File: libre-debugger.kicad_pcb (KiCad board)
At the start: 2 copper layers, 50 x 60 mm, 82 parts, among them J1 USB_C_Receptacle_USB2.0, J2 Conn_ST_STDC14, J4 Conn_01x16, Q1 2N7002, SW1 SW_SPDT, SW2 SW_Push, U1 FT2232H, U10 74LVC1G125, U11 74LVC1G125, U12 74LVC1G125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

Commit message: Replace LDO: MIC5504 -> XC6026
Available on JLCPCB as Basic Part.
Many alternative MPNs available for this new footprint, so not an issue.
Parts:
- U2: value MIC5504-3.3YM5 -> XC6206PxxxMR; footprint Package_TO_SOT_SMD:SOT-23-5 -> Package_TO_SOT_SMD:SOT-23
- moved U2 0.30 mm to (134.4, 60.1), turned to 180 degrees
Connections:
- U2 pad 1: +5V -> GND
- U2 pad 2: GND -> +3V3
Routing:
- net +5V: track 7.08 -> 3.69 mm
- net +3V3: track 14.6 -> 13.0 mm

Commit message: Use 4u7 caps for LDO input and output too
Minimum size recommended is 1uF input and 1uF output.
But given capacitance derating vs DC voltage, it is probably
a good idea to go for a higher value. That reduces the number
of MPNs too.
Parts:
- C1, C2: value 1u -> 4u7
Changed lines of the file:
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@@
       (effects (font (size 0.8 0.8) (thickness 0.15)))
     )
-    (fp_text value "1u" (at 0 1.43 90) (layer "F.Fab") hide
+    (fp_text value "4u7" (at 0 1.43 90) (layer "F.Fab") hide
       (effects (font (size 0.5 0.5) (thickness 0.15)))
     )
@@
       (effects (font (size 0.8 0.8) (thickness 0.15)))
     )
-    (fp_text value "1u" (at 0 1.43 90) (layer "F.Fab") hide
+    (fp_text value "4u7" (at 0 1.43 90) (layer "F.Fab") hide
       (effects (font (size 0.5 0.5) (thickness 0.15)))
     )

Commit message: Layout clean up
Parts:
- turned R8 to 90 degrees
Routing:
- net /GPIO0: track 39.8 -> 37.8 mm
- net /RX_LED_N: track 25.5 -> 24.4 mm
- net /GPIO3: track 41.4 -> 42.2 mm
- net /GPIO1: track 40.1 -> 39.3 mm
- net /TMS_TRGT: track 39.1 -> 38.4 mm
- net /TDI_TRGT: track 51.7 -> 51.2 mm
- net /GPIO2: track 40.4 -> 40.9 mm

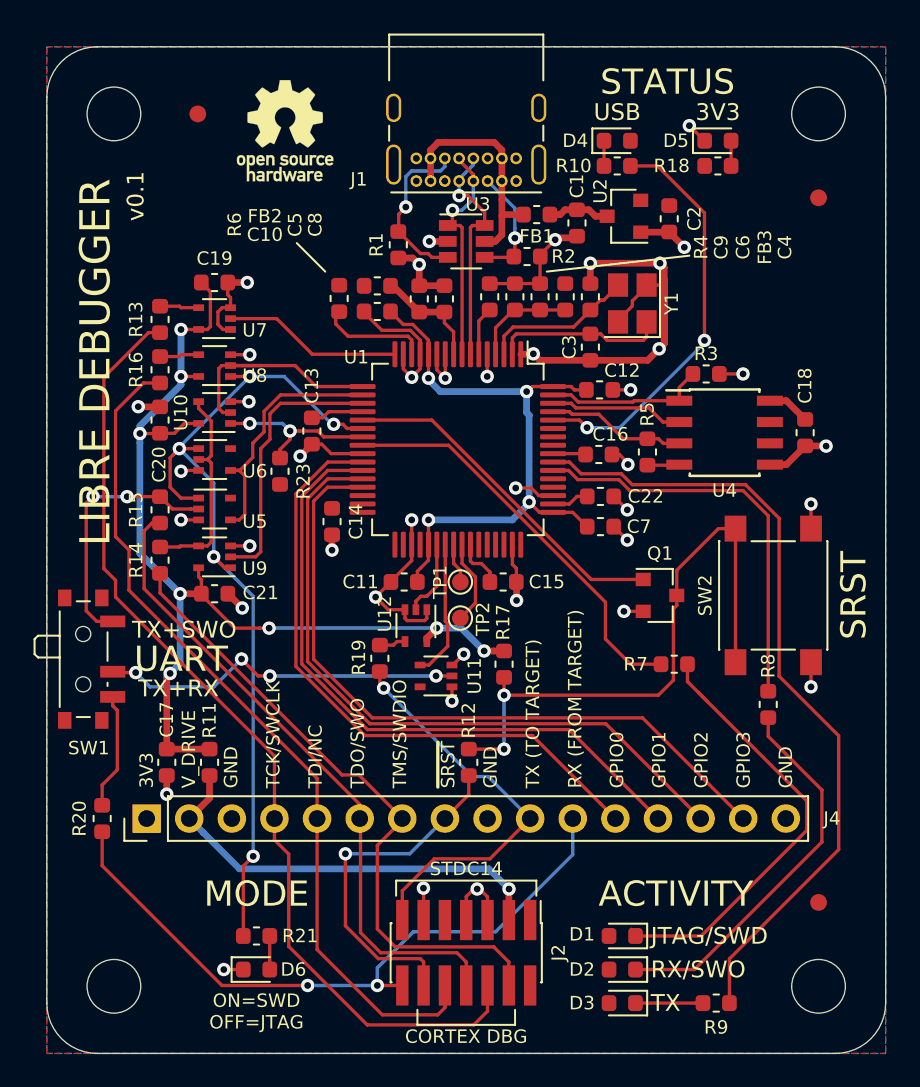
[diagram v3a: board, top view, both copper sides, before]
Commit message: Many layout clean ups including smaller tracks and vias
Now 0.15mm tracks and 0.6mm/0.3mm vias by default.
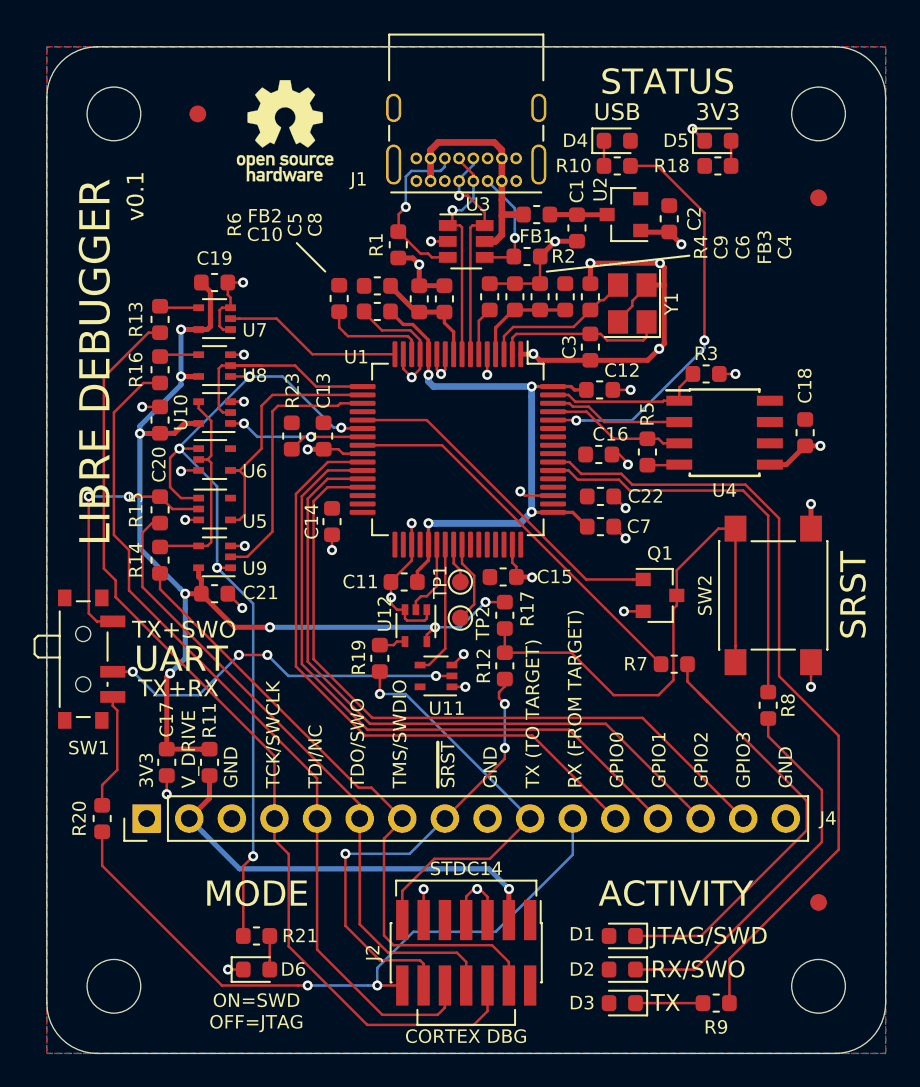
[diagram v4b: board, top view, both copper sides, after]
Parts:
- moved R12 6.14 mm to (127.3, 86.9)
- moved R17 2.91 mm to (127.3, 83.9)
- moved R23 2.21 mm to (114.6, 73.2), turned to 90 degrees
- moved C13 0.76 mm to (116.5, 73.2)
- moved C15 0.30 mm to (127.2, 81.6)
- moved C1 0.30 mm to (131.6, 60.8)
- moved U2 0.10 mm to (134.4, 60.0)
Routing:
- net +3V3: track 13.0 -> 0.17 mm
- net GND: track 116.1 -> 105.0 mm
- net /SRST_N_TRGT: track 21.2 -> 28.1 mm, vias 1 -> 3
- net /SRST_N_R: track 36.0 -> 32.0 mm, vias 2 -> 0
- net /MPSSE_LED_N: track 24.5 -> 23.2 mm
- net /RXD_IN: track 21.8 -> 22.4 mm
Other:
- net class Default: trace_width 0.2 -> 0.15; via_dia 0.8 -> 0.6; via_drill 0.4 -> 0.3
- net class Power: trace_width 0.4 -> 0.3; via_dia 0.8 -> 0.6; via_drill 0.4 -> 0.3
- rule via_min_drill: 0.4 -> 0.3
- rule via_min_size: 0.8 -> 0.6

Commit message: More small layout clean up
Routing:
- net /SRST_N_R: track 32.0 -> 31.2 mm
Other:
- board text added: "Add KiCad logo!!"
- board text added: "FTDI chip CHANNEL A/0 = JTAG/SWD + GPIOs CHANNEL B/1 = UART"
- board text removed: "CHANNEL A/0 = JTAG/SWD + GPIOs CHANNEL B/1 = UART"

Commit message: Add KiCad logo + small improvements
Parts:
- added REF**: KiCad-Logo2_5mm_SilkScreen, Symbol:KiCad-Logo2_5mm_SilkScreen, B.Cu at (108.7, 60.5)
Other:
- board text added: "FTDI chip: CHANNEL A = JTAG/SWD + GPIOs CHANNEL B = UART"
- board text removed: "Add KiCad logo!!"
- board text removed: "FTDI chip CHANNEL A/0 = JTAG/SWD + GPIOs CHANNEL B/1 = UART"
